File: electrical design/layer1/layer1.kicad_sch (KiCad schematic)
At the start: 210 parts, among them J1 XT60-F, J4 XT30PW-F, J5 Conn_01x01_Socket, J6 Conn_01x01_Socket, J7 Conn_01x01_Socket, J8 Conn_01x01_Socket, Q1 MOSFET-NCH-FQP30N06L, Q2 MOSFET-NCH-AO3404A, SW1 SW_DPDT_x2, U1 CD74HC4067SM, U2 CD74HC4067SM, U3 MOUDLE-SEEEDUINO-XIAO-ESP32C3

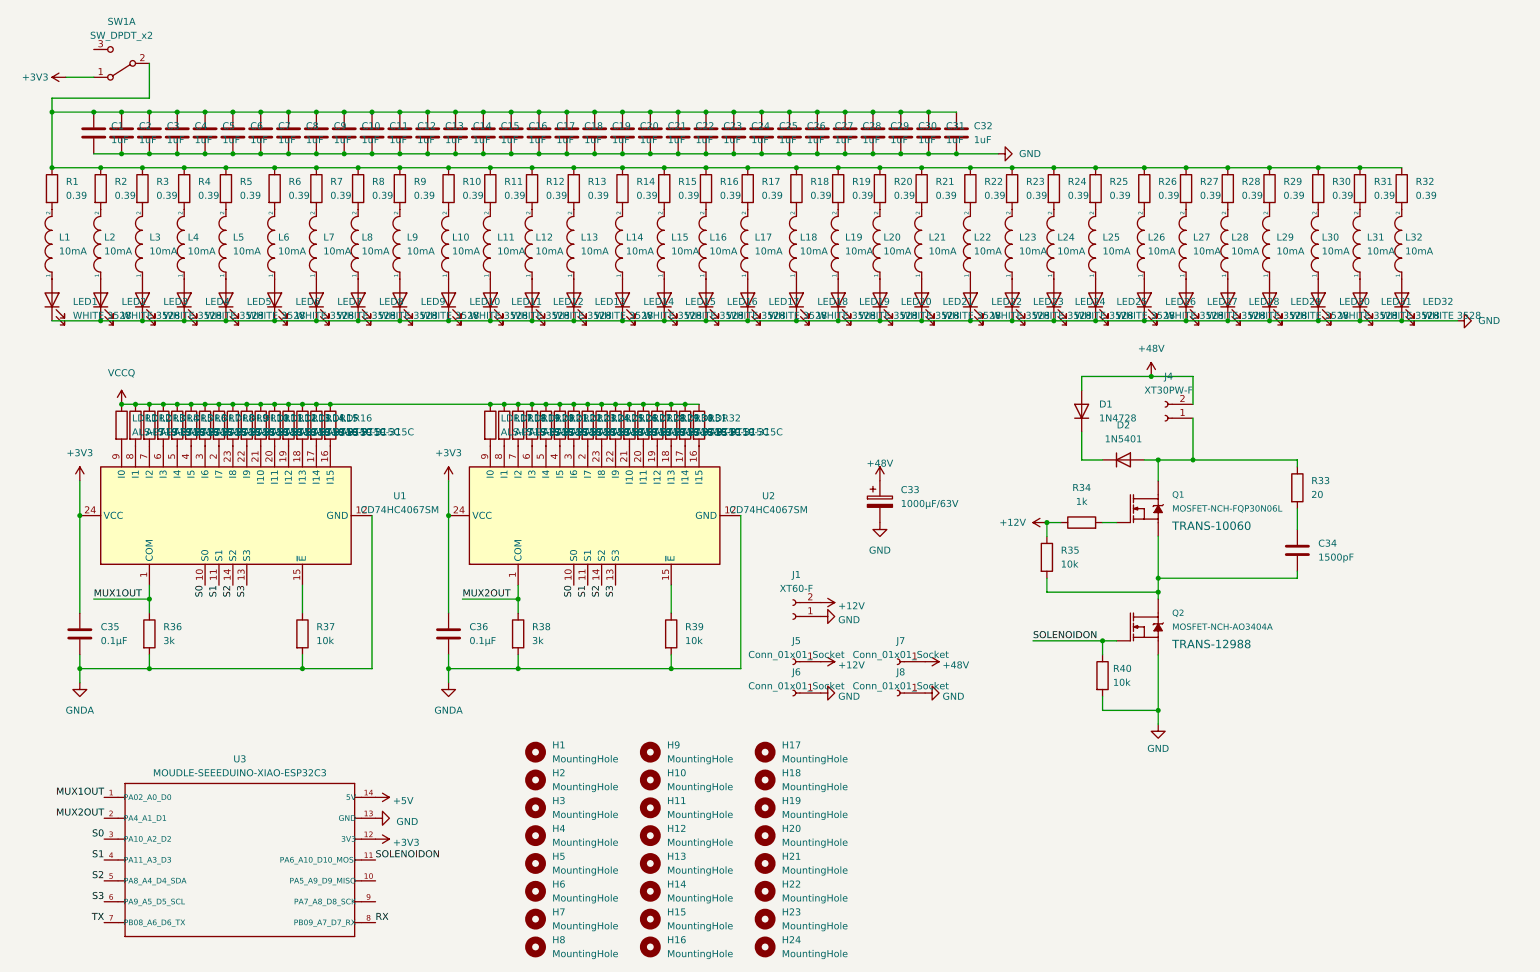
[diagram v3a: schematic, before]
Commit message: reposition kicker circuit and improve routing
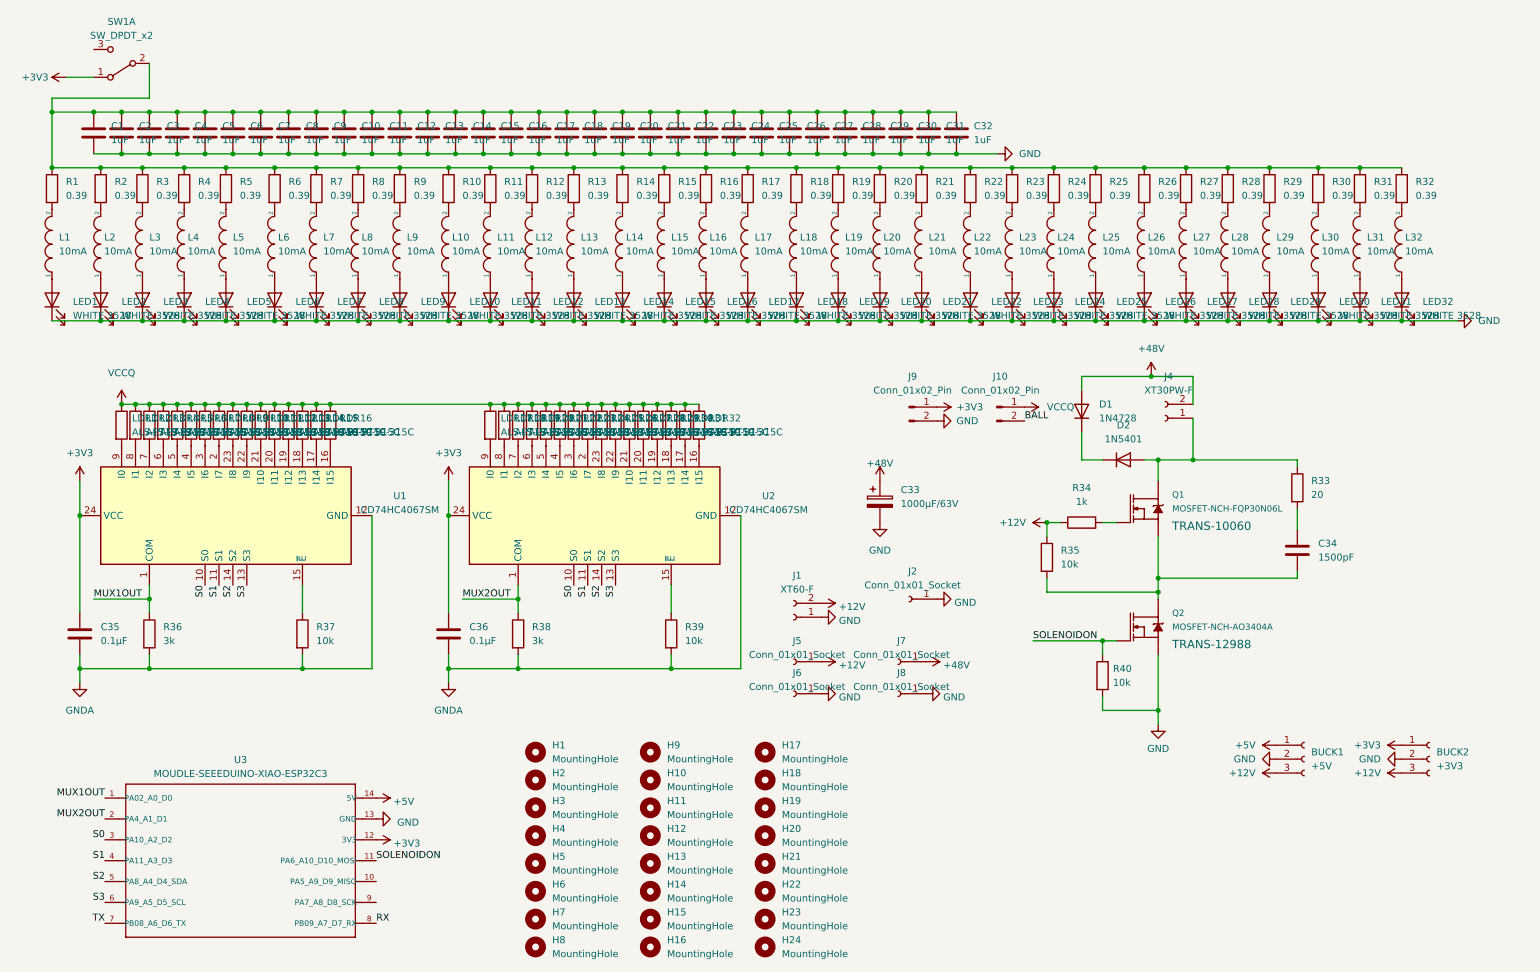
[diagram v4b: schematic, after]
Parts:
- added BUCK1: +5V, Connector_PinHeader_2.54mm:PinHeader_1x03_P2.54mm_Vertical, symbol Connector:Conn_01x03_Female
- added BUCK2: +3V3, Connector_PinHeader_2.54mm:PinHeader_1x03_P2.54mm_Vertical, symbol Connector:Conn_01x03_Female
- added J10, J9: Conn_01x02_Pin, Connector_PinHeader_2.54mm:PinHeader_1x02_P2.54mm_Vertical, symbol Connector:Conn_01x02_Pin
- added J2: Conn_01x01_Socket, Connector_Wire:SolderWire-0.75sqmm_1x01_D1.25mm_OD2.3mm, symbol Connector:Conn_01x01_Socket
- J4: footprint Connector_AMASS:AMASS_XT30PW-F_1x02_P2.50mm_Horizontal -> Connector_AMASS:AMASS_XT30UPB-F_1x02_P5.0mm_Vertical
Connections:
- net +12V: now also BUCK1.3 (Pin_3), BUCK2.3 (Pin_3)
- net +3V3: now also BUCK2.1 (Pin_1), J9.1 (Pin_1)
- net +5V: now also BUCK1.1 (Pin_1)
- net GND: now also BUCK1.2 (Pin_2), BUCK2.2 (Pin_2), J2.1 (Pin_1), J9.2 (Pin_2)
- net VCCQ: now also J10.1 (Pin_1)
- new net BALL: J10.2 (Pin_2)

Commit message: update layer 1 design files
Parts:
- added J11: Conn_01x01_Socket, Connector_Wire:SolderWirePad_1x01_SMD_1x2mm, symbol Connector:Conn_01x01_Socket
- added J12: Conn_01x01_Socket, Connector_Wire:SolderWire-0.5sqmm_1x01_D0.9mm_OD2.1mm, symbol Connector:Conn_01x01_Socket
- added J13: Conn_01x05_Pin, Connector_JST:JST_SH_BM05B-SRSS-TB_1x05-1MP_P1.00mm_Vertical, symbol Connector:Conn_01x05_Pin
- added J14: Conn_01x02_Pin, Connector_JST:JST_SH_BM02B-SRSS-TB_1x02-1MP_P1.00mm_Vertical, symbol Connector:Conn_01x02_Pin
- added J3: Conn_01x01_Socket, Connector_Wire:SolderWirePad_1x01_SMD_5x10mm, symbol Connector:Conn_01x01_Socket
- added TP1, TP2, TP3, TP4: TestPoint_2Pole, TestPoint:TestPoint_2Pads_Pitch2.54mm_Drill0.8mm, symbol Connector:TestPoint_2Pole
- BUCK1: value +5V -> VCCQ; footprint Connector_PinHeader_2.54mm:PinHeader_1x03_P2.54mm_Vertical -> Connector_PinSocket_2.54mm:PinSocket_1x03_P2.54mm_Horizontal
- BUCK2: footprint Connector_PinHeader_2.54mm:PinHeader_1x03_P2.54mm_Vertical -> Connector_PinSocket_2.54mm:PinSocket_1x03_P2.54mm_Horizontal
- J1: value XT60-F -> XT30-F
- J2: footprint Connector_Wire:SolderWire-0.75sqmm_1x01_D1.25mm_OD2.3mm -> Connector_Wire:SolderWirePad_1x01_SMD_1x2mm
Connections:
- net +12V: now also J3.1 (Pin_1), TP2.1
- net +3V3: now also J13.3 (Pin_3), TP4.1
- net +48V: now also TP1.1
- net +5V: now also J13.1 (Pin_1); no longer BUCK1.1 (Pin_1)
- net BALL: now also U3.10 (PA5_A9_D9_MISO)
- net GND: now also TP1.2, TP2.2, TP3.2, TP4.2; no longer U3.13 (GND)
- net GNDA: now also J14.1 (Pin_1)
- net RX: now also J13.4 (Pin_4)
- net TX: now also J13.5 (Pin_5)
- net VCCQ: now also BUCK1.1 (Pin_1), TP3.1
- net LED: now reaches C1.1, C10.1, C11.1, C12.1, C13.1, C14.1, C15.1, C16.1, C17.1, C18.1, C19.1, C2.1, C20.1, C21.1, C22.1, C23.1, C24.1, C25.1, C26.1, C27.1, C28.1, C29.1, C3.1, C30.1, C31.1, C32.1, C4.1, C5.1, C6.1, C7.1, C8.1, C9.1, R1.1, R10.1, R11.1, R12.1, R13.1, R14.1, R15.1, R16.1, R17.1, R18.1, R19.1, R2.1, R20.1, R21.1, R22.1, R23.1, R24.1, R25.1, R26.1, R27.1, R28.1, R29.1, R3.1, R30.1, R31.1, R32.1, R4.1, R5.1, R6.1, R7.1, R8.1, R9.1, SW1.2 (B)
- net LED: now also J11.1 (Pin_1), J12.1 (Pin_1)
- new net GNDD: J13.2 (Pin_2), J14.2 (Pin_2), U3.13 (GND)
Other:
- moved on the sheet: BUCK2, J1, J10, J5, J6, J7, J8, J9, U3

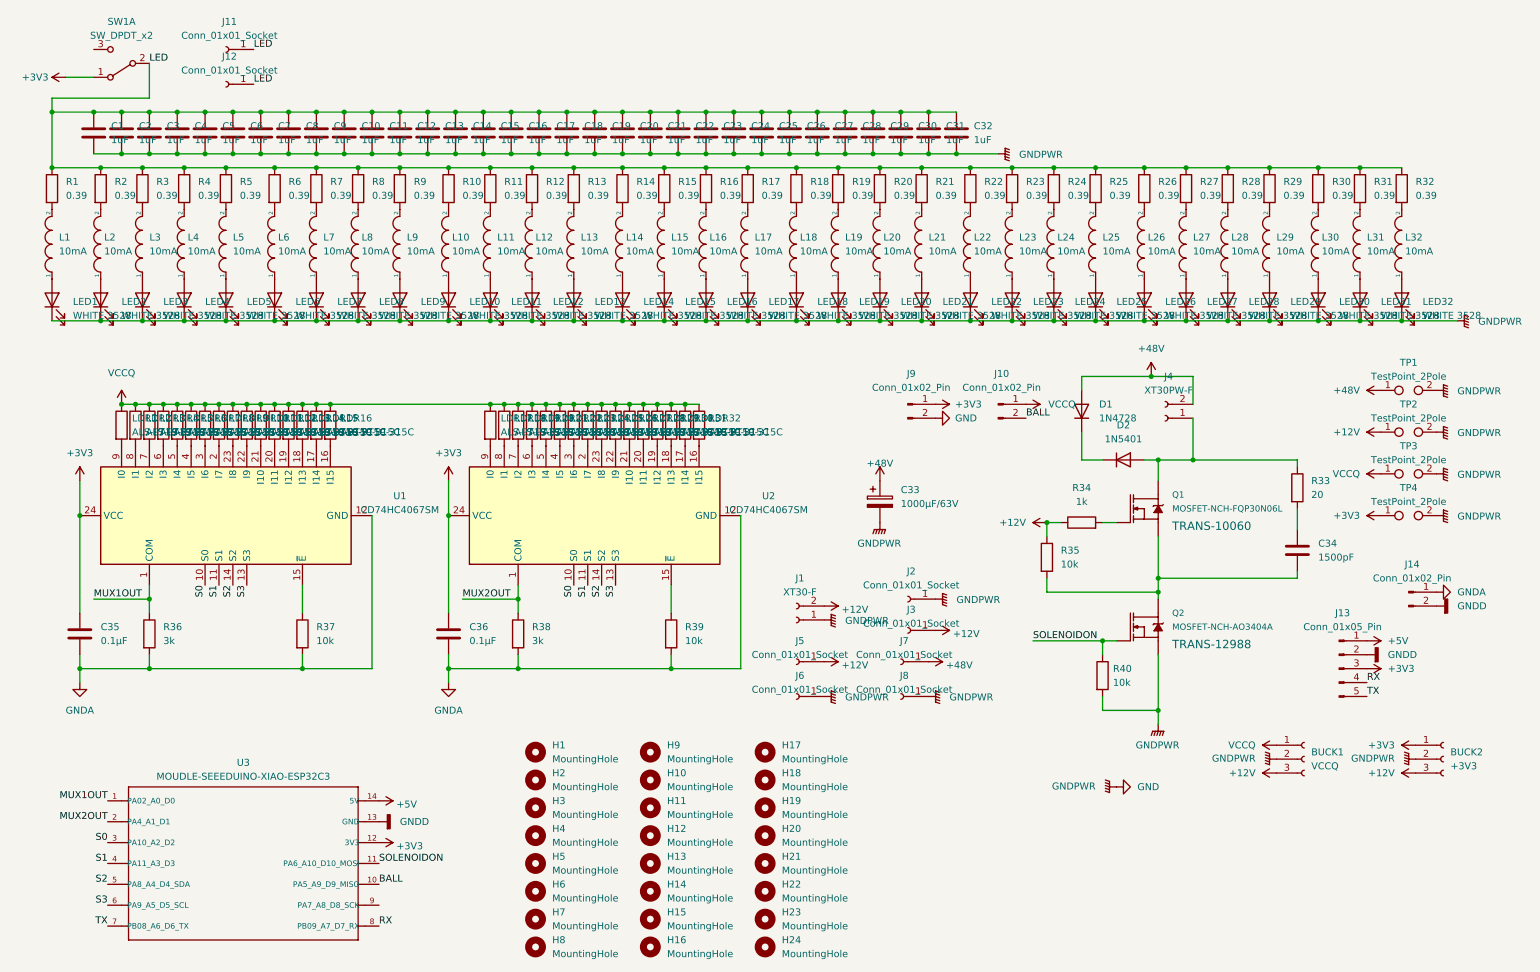
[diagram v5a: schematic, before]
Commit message: add fb between vccq and 3v3
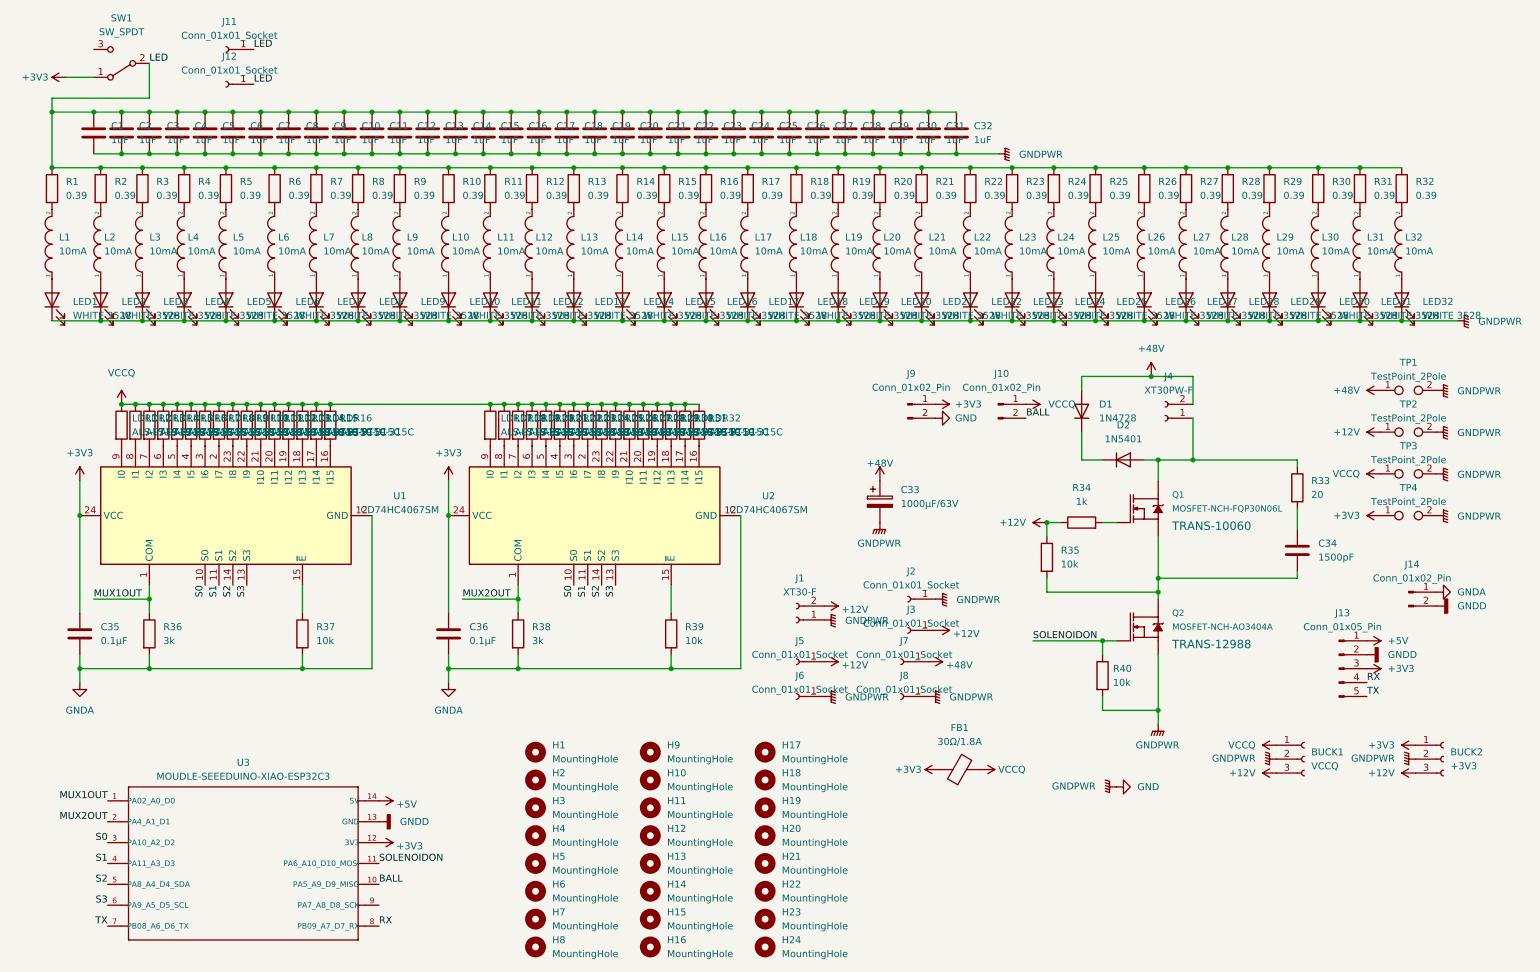
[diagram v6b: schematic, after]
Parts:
- removed SW1: SW_DPDT_x2, Switches:SWITCH_SPDT_PTH_11.6X4.0MM_LOCK, symbol Switch:SW_DPDT_x2
- added FB1: 30Ω/1.8A, Capacitor_SMD:C_0603_1608Metric, symbol Device:FerriteBead
- added SW1: SW_SPDT, Switches:SWITCH_SPDT_PTH_11.6X4.0MM, symbol Switch:SW_SPDT
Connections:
- net +3V3: now also FB1.1, SW1.1 (A)
- net LED: now also SW1.2 (B)
- net VCCQ: now also FB1.2
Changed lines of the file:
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@@
     )
   )
+  (symbol (lib_name "VCCQ_4") (lib_id "power:VCCQ") (at 191.135 155.575 270) (unit 1)
+    (in_bom yes) (on_board yes) (dnp no) (fields_autoplaced)
+    (property "Reference" "#PWR046" (at 187.325 155.575 0)
+      (effects (font (size 1.27 1.27)) hide)
+    )
+    (property "Value" "VCCQ" (at 194.31 155.575 90)
+      (effects (font (size 1.27 1.27)) (justify left))
+    )
+    (property "Footprint" "" (at 191.135 155.575 0)
+      (effects (font (size 1.27 1.27)) hide)
+    )
+    (property "Datasheet" "" (at 191.135 155.575 0)
+      (effects (font (size 1.27 1.27)) hide)
+    )
+    (pin "1")
+    (instances
+      (project "layer1"
+        (path "/32d54464-fd6f-441d-9cef-d3e4fabf9fe1"
+          (reference "#PWR046") (unit 1)
+        )
+      )
+    )
+  )
   (symbol (lib_id "Device:LED") (at 260.35 69.85 90) (unit 1)
     (in_bom yes) (on_board yes) (dnp no) (fields_autoplaced)
@@
     )
   )
+  (symbol (lib_name "+3V3_4") (lib_id "power:+3V3") (at 183.515 155.575 90) (unit 1)
+    (in_bom yes) (on_board yes) (dnp no) (fields_autoplaced)
+    (property "Reference" "#PWR047" (at 187.325 155.575 0)
+      (effects (font (size 1.27 1.27)) hide)
+    )
+    (property "Value" "+3V3" (at 180.34 155.575 90)
+      (effects (font (size 1.27 1.27)) (justify left))
+    )
+    (property "Footprint" "" (at 183.515 155.575 0)
+      (effects (font (size 1.27 1.27)) hide)
+    )
+    (property "Datasheet" "" (at 183.515 155.575 0)
+      (effects (font (size 1.27 1.27)) hide)
+    )
+    (pin "1")
+    (instances
+      (project "layer1"
+        (path "/32d54464-fd6f-441d-9cef-d3e4fabf9fe1"
+          (reference "#PWR047") (unit 1)
+        )
+      )
+    )
+  )
   (symbol (lib_id "pspice:INDUCTOR") (at 267.97 59.69 90) (unit 1)
     (in_bom yes) (on_board yes) (dnp no) (fields_autoplaced)
@@
     )
   )
+  (symbol (lib_id "Switch:SW_SPDT") (at 34.29 26.67 180) (unit 1)
+    (in_bom yes) (on_board yes) (dnp no) (fields_autoplaced)
+    (property "Reference" "SW1" (at 34.29 18.415 0)
+      (effects (font (size 1.27 1.27)))
+    )
+    (property "Value" "SW_SPDT" (at 34.29 20.955 0)
+      (effects (font (size 1.27 1.27)))
+    )
+    (property "Footprint" "Switches:SWITCH_SPDT_PTH_11.6X4.0MM" (at 34.29 26.67 0)
+      (effects (font (size 1.27 1.27)) hide)
+    )
+    (property "Datasheet" "~" (at 34.29 26.67 0)
+      (effects (font (size 1.27 1.27)) hide)
+    )
+    (pin "2")
+    (pin "1")
+    (pin "3")
+    (instances
+      (project "layer1"
+        (path "/32d54464-fd6f-441d-9cef-d3e4fabf9fe1"
+          (reference "SW1") (unit 1)
+        )
+      )
+      (project "layer3"
+        (path "/e63e39d7-6ac0-4ffd-8aa3-1841a4541b55"
+          (reference "SW1") (unit 1)
+        )
+      )
+    )
+  )
   (symbol (lib_id "pspice:INDUCTOR") (at 38.1 59.69 90) (unit 1)
     (in_bom yes) (on_board yes) (dnp no) (fields_autoplaced)
@@
     )
   )
+  (symbol (lib_id "Device:FerriteBead") (at 187.325 155.575 90) (unit 1)
+    (in_bom yes) (on_board yes) (dnp no) (fields_autoplaced)
+    (property "Reference" "FB1" (at 187.2742 147.955 90)
+      (effects (font (size 1.27 1.27)))
+    )
+    (property "Value" "30Ω/1.8A" (at 187.2742 150.495 90)
+      (effects (font (size 1.27 1.27)))
+    )
+    (property "Footprint" "Capacitor_SMD:C_0603_1608Metric" (at 187.325 157.353 90)
+      (effects (font (size 1.27 1.27)) hide)
+    )
+    (property "Datasheet" "~" (at 187.325 155.575 0)
+      (effects (font (size 1.27 1.27)) hide)
+    )
+    (pin "1")
+    (pin "2")
+    (instances
+      (project "layer1"
+        (path "/32d54464-fd6f-441d-9cef-d3e4fabf9fe1"
+          (reference "FB1") (unit 1)
+        )
+      )
+      (project "layer1"
+        (path "/ceef7b68-a05c-4136-9e96-66c3c7de2b7e"
+          (reference "FB1") (unit 1)
+        )
+      )
+    )
+  )
   (symbol (lib_id "Device:R") (at 134.62 92.71 0) (unit 1)
     (in_bom yes) (on_board yes) (dnp no) (fields_autoplaced)
@@
         )
       )
-    )
-  )
-  (symbol (lib_id "Switch:SW_DPDT_x2") (at 34.29 26.67 180) (unit 1)
-    (in_bom yes) (on_board yes) (dnp no) (fields_autoplaced)
-    (property "Reference" "SW1" (at 34.29 19.05 0)
-      (effects (font (size 1.27 1.27)))
-    )
-    (property "Value" "SW_DPDT_x2" (at 34.29 21.59 0)
-      (effects (font (size 1.27 1.27)))
-    )
-    (property "Footprint" "Switches:SWITCH_SPDT_PTH_11.6X4.0MM_LOCK" (at 34.29 26.67 0)
-      (effects (font (size 1.27 1.27)) hide)
-    )
-    (property "Datasheet" "~" (at 34.29 26.67 0)
-      (effects (font (size 1.27 1.27)) hide)
-    )
-    (pin "1")
-    (pin "2")
-    (pin "3")
-    (pin "4")
-    (pin "5")
-    (pin "6")
-    (instances
-      (project "layer1"
-        (path "/32d54464-fd6f-441d-9cef-d3e4fabf9fe1"
-          (reference "SW1") (unit 1)
-        )
-      )
